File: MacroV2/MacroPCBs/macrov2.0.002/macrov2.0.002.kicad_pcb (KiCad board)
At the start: 2 copper layers, 120 x 85 mm, 46 parts, among them J1 Conn_01x15_Pin, SW1 RotaryEncoder_Switch, SW2 RotaryEncoder_Switch, SW3 SW_Push, U1 Raspberry_Pi_Pico

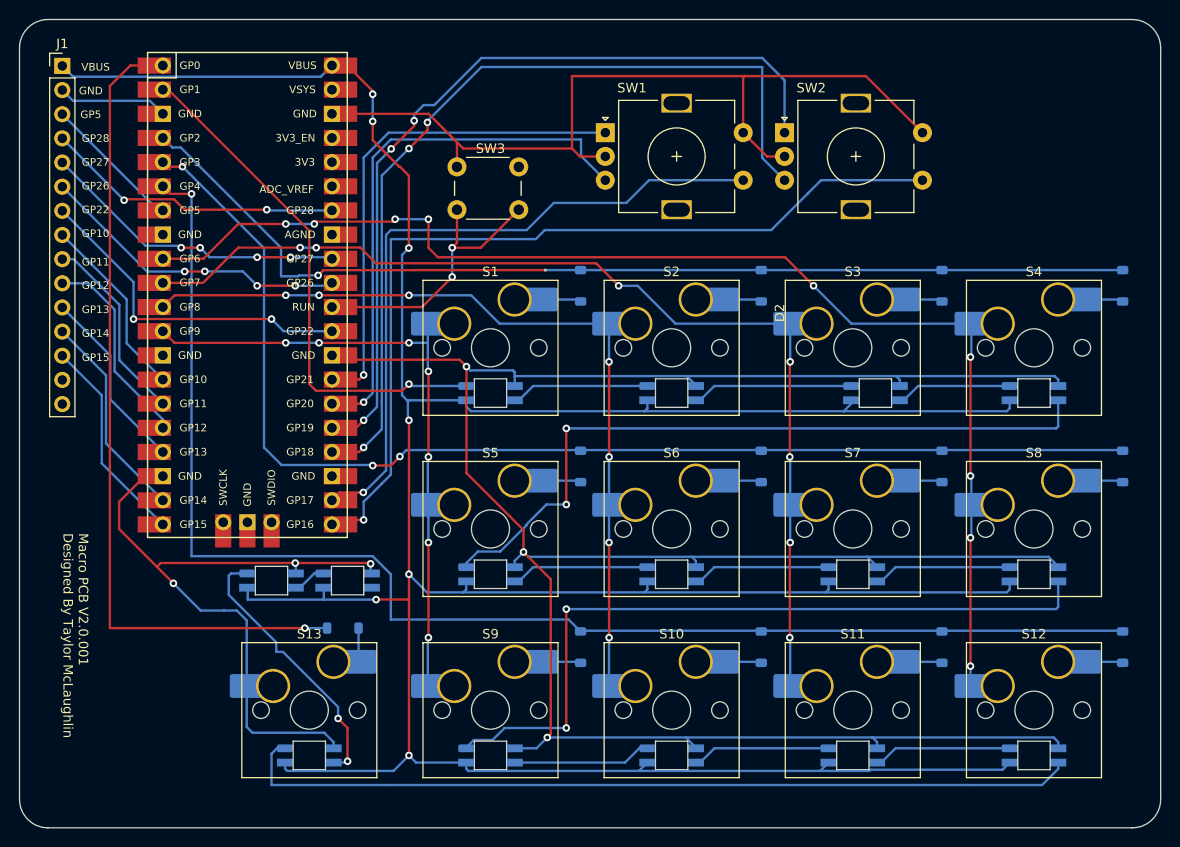
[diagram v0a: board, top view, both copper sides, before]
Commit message: PCB revisions, Newest is in production
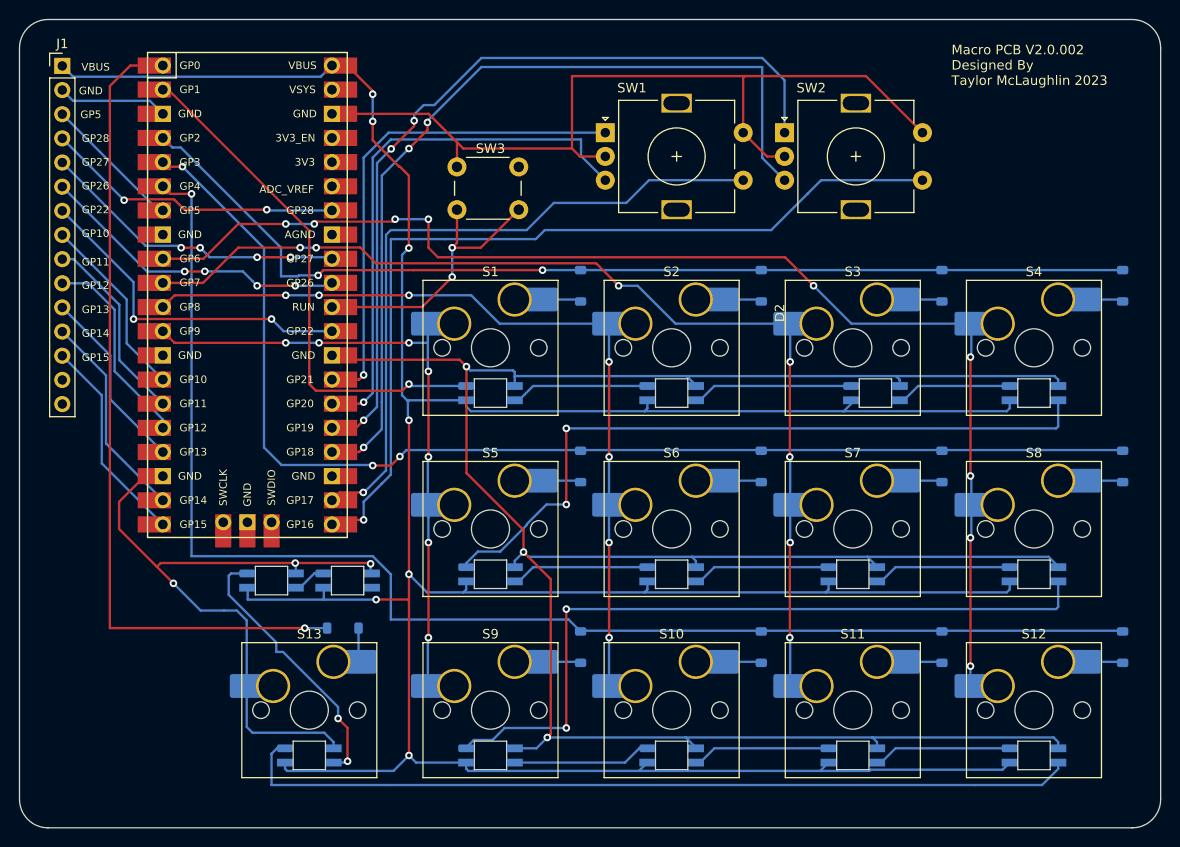
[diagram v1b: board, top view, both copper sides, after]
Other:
- board text added: "Macro PCB V2.0.002 Designed By Taylor McLaughlin 2023"
- board text removed: "Macro PCB V2.0.001 Designed By Taylor McLaughlin"
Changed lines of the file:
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@@
     (title "Macro PCB")
     (date "2023-12-19")
-    (rev "2.0.001")
+    (rev "2.0.002")
   )
   (layers
@@
     (effects (font (size 0.8 0.8) (thickness 0.15)))
   )
-  (gr_text "Macro PCB V2.0.001\nDesigned By Taylor McLaughlin" (at 61.415 72.4975 -90) (layer "F.SilkS")
+  (gr_text "Macro PCB V2.0.002\nDesigned By \nTaylor McLaughlin 2023" (at 154.915 25.4975) (layer "F.SilkS")
     (effects (font (size 1 1) (thickness 0.15)) (justify left bottom))
   )
@@
     (effects (font (size 0.8 0.8) (thickness 0.15)))
   )
-  (segment (start 112.210044 44.847) (end 112.210546 44.847502) (width 0.25) (layer "F.Cu") (net 1))
   (segment (start 88.86651 44.857738) (end 88.321748 45.4025) (width 0.25) (layer "F.Cu") (net 1))
-  (segment (start 98.363727 44.847) (end 112.210044 44.847) (width 0.25) (layer "F.Cu") (net 1))
+  (segment (start 111.904762 44.847) (end 98.363727 44.847) (width 0.25) (layer "F.Cu") (net 1))
   (segment (start 98.352989 44.857738) (end 98.363727 44.847) (width 0.25) (layer "F.Cu") (net 1))
+  (segment (start 111.915 44.857238) (end 111.904762 44.847) (width 0.25) (layer "F.Cu") (net 1))
   (segment (start 98.352989 44.857738) (end 88.86651 44.857738) (width 0.25) (layer "F.Cu") (net 1))
-  (via micro (at 112.210546 44.847502) (size 0.3) (drill 0.1) (layers "F.Cu" "B.Cu") (net 1))
+  (via (at 111.915 44.857238) (size 0.8) (drill 0.4) (layers "F.Cu" "B.Cu") (net 1))
   (via (at 88.321748 45.4025) (size 0.8) (drill 0.4) (layers "F.Cu" "B.Cu") (net 1))
   (segment (start 72.99125 31.95625) (end 71.99125 30.95625) (width 0.25) (layer "B.Cu") (net 1))
   (segment (start 88.321748 45.4025) (end 86.294695 45.4025) (width 0.25) (layer "B.Cu") (net 1))
-  (segment (start 112.210548 44.8475) (end 115.915 44.8475) (width 0.25) (layer "B.Cu") (net 1))
+  (segment (start 115.915 44.8475) (end 111.924738 44.8475) (width 0.25) (layer "B.Cu") (net 1))
   (segment (start 84.415 42.4975) (end 73.87375 31.95625) (width 0.25) (layer "B.Cu") (net 1))
   (segment (start 172.915 44.8475) (end 115.915 44.8475) (width 0.25) (layer "B.Cu") (net 1))
   (segment (start 86.294695 45.4025) (end 86.199695 45.4975) (width 0.25) (layer "B.Cu") (net 1))
-  (segment (start 112.210546 44.847502) (end 112.210548 44.8475) (width 0.25) (layer "B.Cu") (net 1))
   (segment (start 84.415 45.4975) (end 84.415 42.4975) (width 0.25) (layer "B.Cu") (net 1))
   (segment (start 86.199695 45.4975) (end 84.415 45.4975) (width 0.25) (layer "B.Cu") (net 1))
+  (segment (start 111.924738 44.8475) (end 111.915 44.857238) (width 0.25) (layer "B.Cu") (net 1))
   (segment (start 73.87375 31.95625) (end 72.99125 31.95625) (width 0.25) (layer "B.Cu") (net 1))
   (segment (start 115.71 47.9425) (end 115.915 48.1475) (width 0.25) (layer "B.Cu") (net 2))
